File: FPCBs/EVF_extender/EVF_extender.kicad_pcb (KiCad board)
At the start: 2 copper layers, 2 parts, among them J3 FR02C061JA1-R5000, J4 FPC_2Rows-61Pins_0.2mm

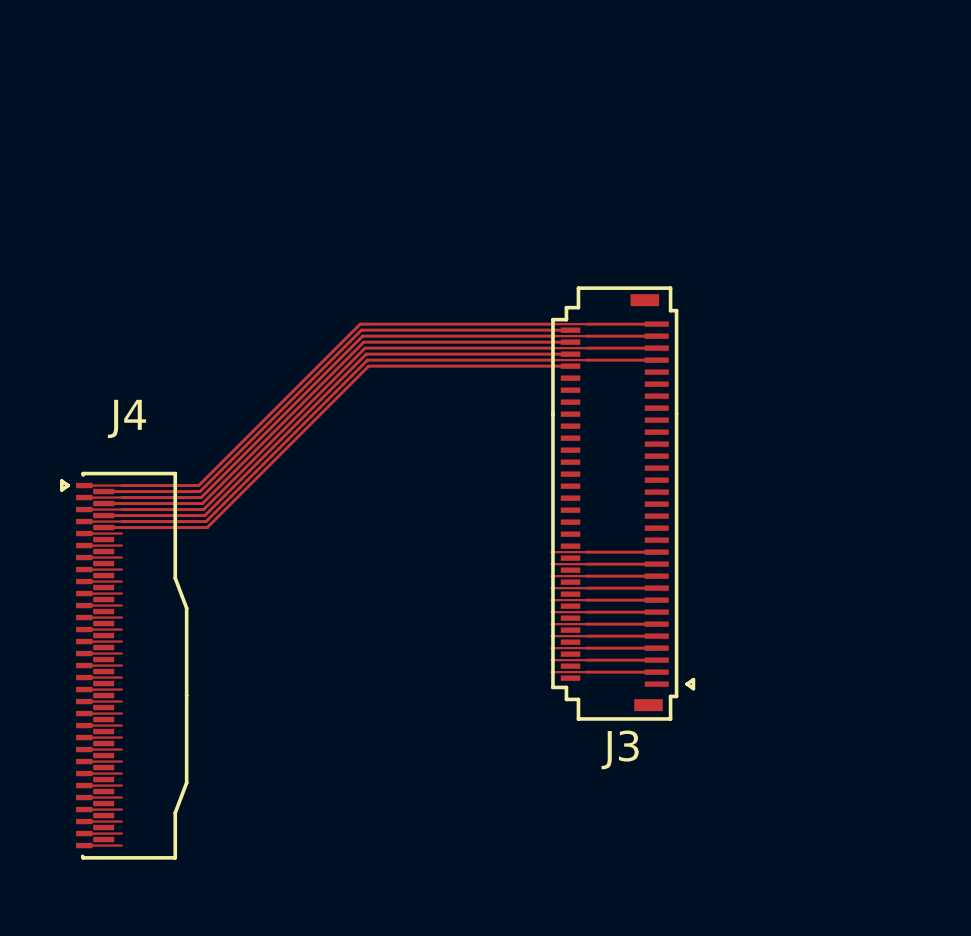
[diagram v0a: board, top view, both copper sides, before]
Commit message: Add EVF extender FPCB
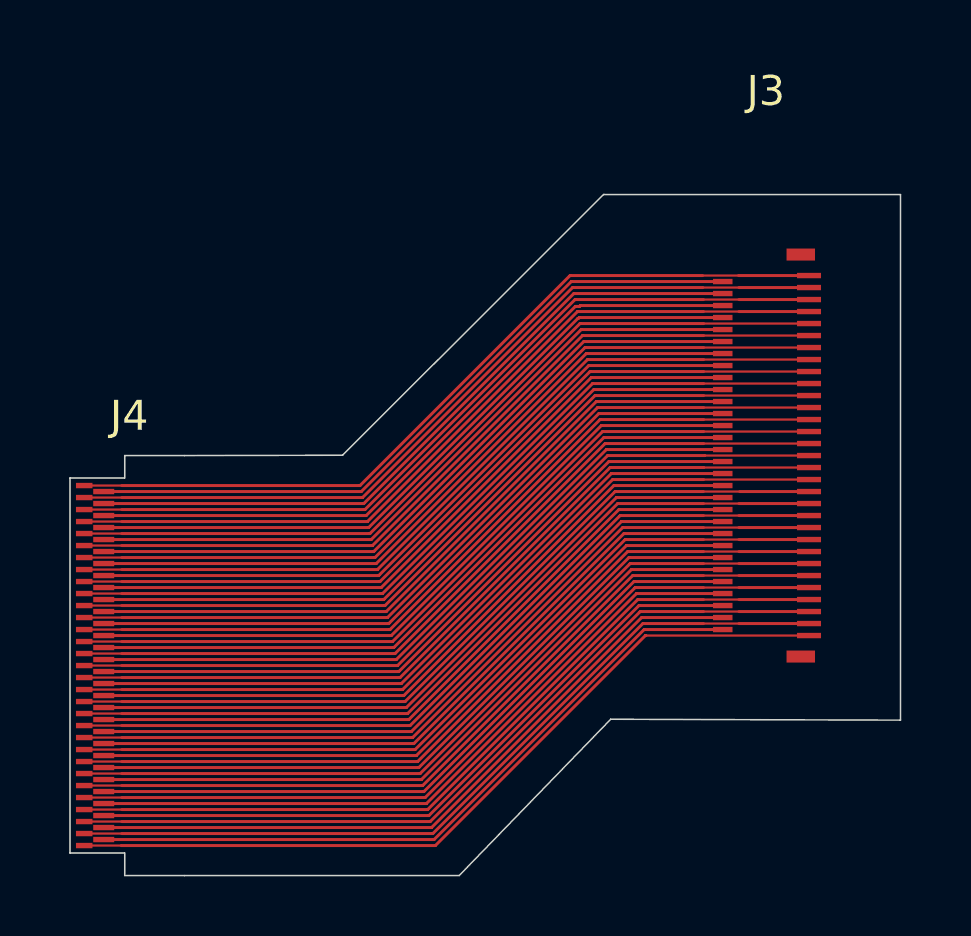
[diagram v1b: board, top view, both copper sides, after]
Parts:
- J3: footprint G9_Connectors:Connector-2Rows-61Pins-0.20mm -> Leica-G9ii:Connector-2Rows-61Pins-0.20mm
- J4: footprint G9_Connectors:FPC-2Rows-61Pins-0.20mm -> Leica-G9ii:FPC-2Rows-61Pins-0.20mm
- moved J3 5.33 mm to (155.5, 78.0)
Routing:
- net Net-(J4-Pin_31): track 1.25 -> 27.1 mm
- net Net-(J4-Pin_33): track 1.25 -> 27.1 mm
- net Net-(J4-Pin_61): track 1.25 -> 27.1 mm
- net Net-(J4-Pin_9): track 1.25 -> 27.1 mm
- net Net-(J4-Pin_37): track 1.25 -> 27.1 mm
- net Net-(J4-Pin_35): track 1.25 -> 27.1 mm
- net Net-(J4-Pin_29): track 1.25 -> 27.1 mm
- net Net-(J4-Pin_27): track 1.25 -> 27.1 mm
- net Net-(J4-Pin_25): track 1.25 -> 27.1 mm
- net Net-(J4-Pin_23): track 1.25 -> 27.1 mm
- net Net-(J4-Pin_21): track 1.25 -> 27.1 mm
- net Net-(J4-Pin_19): track 1.25 -> 27.1 mm
- net Net-(J4-Pin_17): track 1.25 -> 27.1 mm
- net Net-(J4-Pin_15): track 1.25 -> 27.1 mm
- net Net-(J4-Pin_13): track 1.25 -> 27.1 mm
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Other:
- board outline added: 23.9 x 22.7 mm

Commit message: Add curved tracks
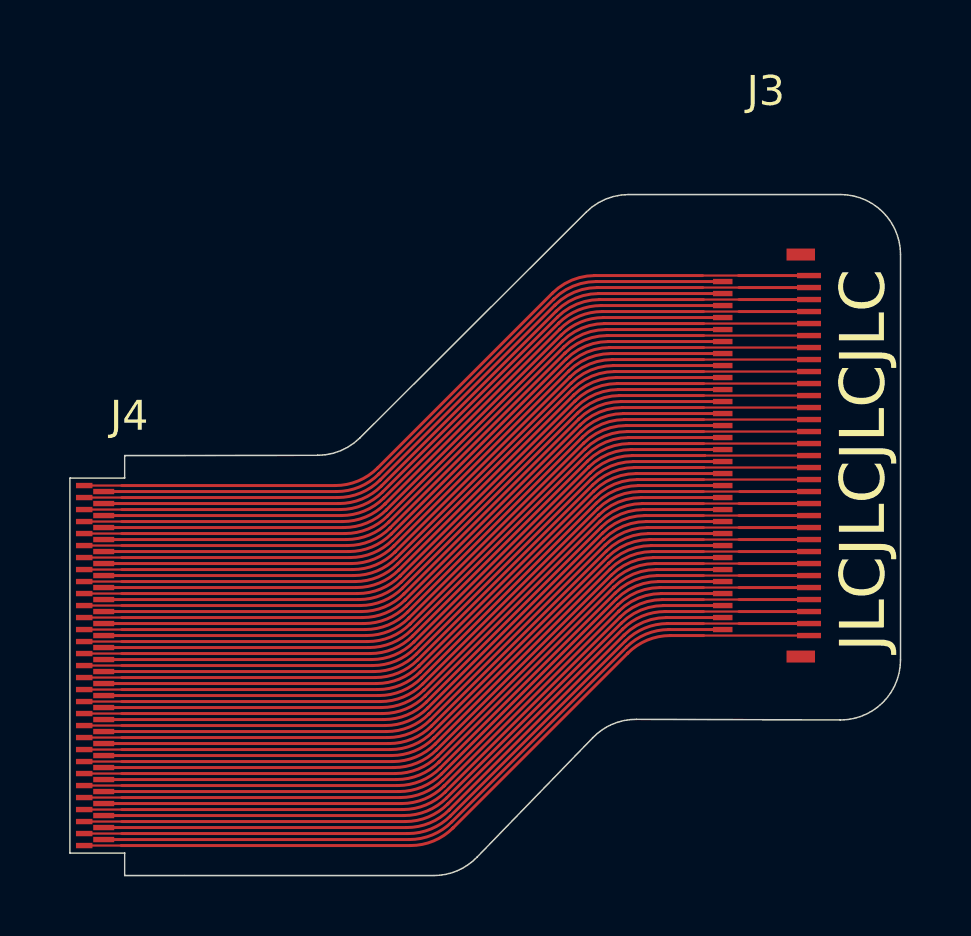
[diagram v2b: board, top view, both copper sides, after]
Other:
- outline, holes or cut-outs redrawn
- board text added: "JLCJLCJLCJLC"
